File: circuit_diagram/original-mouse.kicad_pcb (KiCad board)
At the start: 2 copper layers, 70.4 x 100 mm, 106 parts, among them J1 Conn_02x03_Odd_Even, J2 Conn_02x03_Odd_Even, J3 Conn_01x08, Q1 TJ8S06M3L, Q10 ST-1KL3A, Q2 BSS138, Q3 BSS138, Q4 BSS138, Q5 BSS138, Q6 BSS138, Q7 ST-1KL3A, Q8 ST-1KL3A, Q9 ST-1KL3A, SW1 SW_SPDT, SW2 SW_Push, SW3 SW_Push, SW4 SW_Push, SW5 SW_Push, SW6 SW_Push, U1 NJM7805SDL1, U2 NJM2845DL1-33, U3 PKMCS0909E4000-R1, U4 ICM-20649, U5 DRV8835, U6 STM32F405RGTx

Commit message: 配線完了
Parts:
- moved D2 0.54 mm to (179.5, 115.8)
- moved R6 0.54 mm to (179.5, 114.2)
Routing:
- net VBAT_AD: track 58.3 -> 60.8 mm
- net +3.3V: track 474.7 -> 473.7 mm
- net LEFT_FRONT_AD: track 30.9 -> 30.0 mm
- net LEFT_SIDE: track 24.0 -> 24.7 mm
- net NRST: track 50.4 -> 50.9 mm
- net GND: track 239.9 -> 240.1 mm, vias 108 -> 142

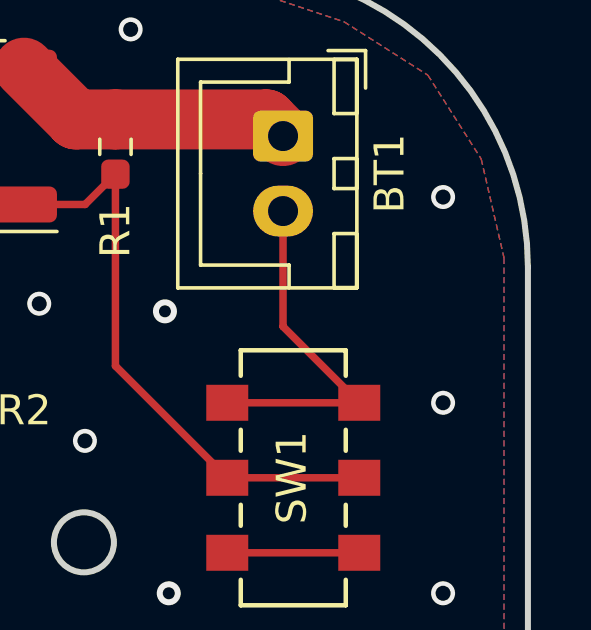
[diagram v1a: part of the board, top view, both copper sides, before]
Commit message: 回路にバージョンを記載
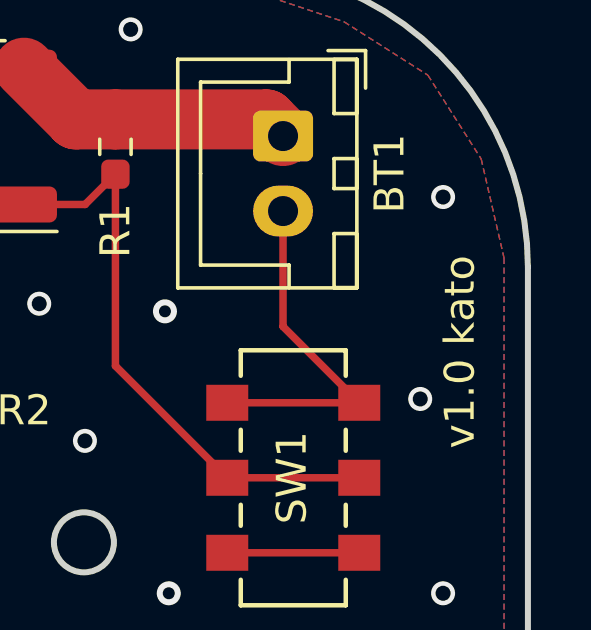
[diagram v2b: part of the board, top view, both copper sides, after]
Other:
- board text added: "v1.0 kato"
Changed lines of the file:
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@@
   (gr_arc locked (start 114.8 99.827683) (mid 115.385792 98.41348) (end 116.8 97.827683)
     (stroke (width 0.2) (type solid)) (layer "Edge.Cuts"))
+  (gr_text "v1.0 kato" (at 183.515 55.372 90) (layer "F.SilkS")
+    (effects (font (size 1 1) (thickness 0.15)) (justify left bottom))
+  )
   (segment (start 177.038 44.958) (end 176.483 44.403) (width 2) (layer "F.Cu") (net 1))
   (segment (start 170.127 44.403) (end 168.402 42.678) (width 2) (layer "F.Cu") (net 1))
@@
   (via (at 182.372 46.99) (size 0.8) (drill 0.5) (layers "F.Cu" "B.Cu") (free) (net 2))
   (via (at 160.782 117.856) (size 0.8) (drill 0.5) (layers "F.Cu" "B.Cu") (free) (net 2))
-  (via (at 182.372 53.848) (size 0.8) (drill 0.5) (layers "F.Cu" "B.Cu") (free) (net 2))
+  (via (at 181.61 53.721) (size 0.8) (drill 0.5) (layers "F.Cu" "B.Cu") (free) (net 2))
   (via (at 170.18 122.682) (size 0.8) (drill 0.5) (layers "F.Cu" "B.Cu") (free) (net 2))
   (via (at 151.892 81.28) (size 0.8) (drill 0.5) (layers "F.Cu" "B.Cu") (net 2))

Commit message: レビューに対応して修正
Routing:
- net +3.3V: track 473.7 -> 472.1 mm
- net BLED0: track 58.6 -> 57.8 mm
